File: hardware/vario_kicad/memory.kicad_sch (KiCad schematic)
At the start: 10 parts, among them U3 W25Q128JVS

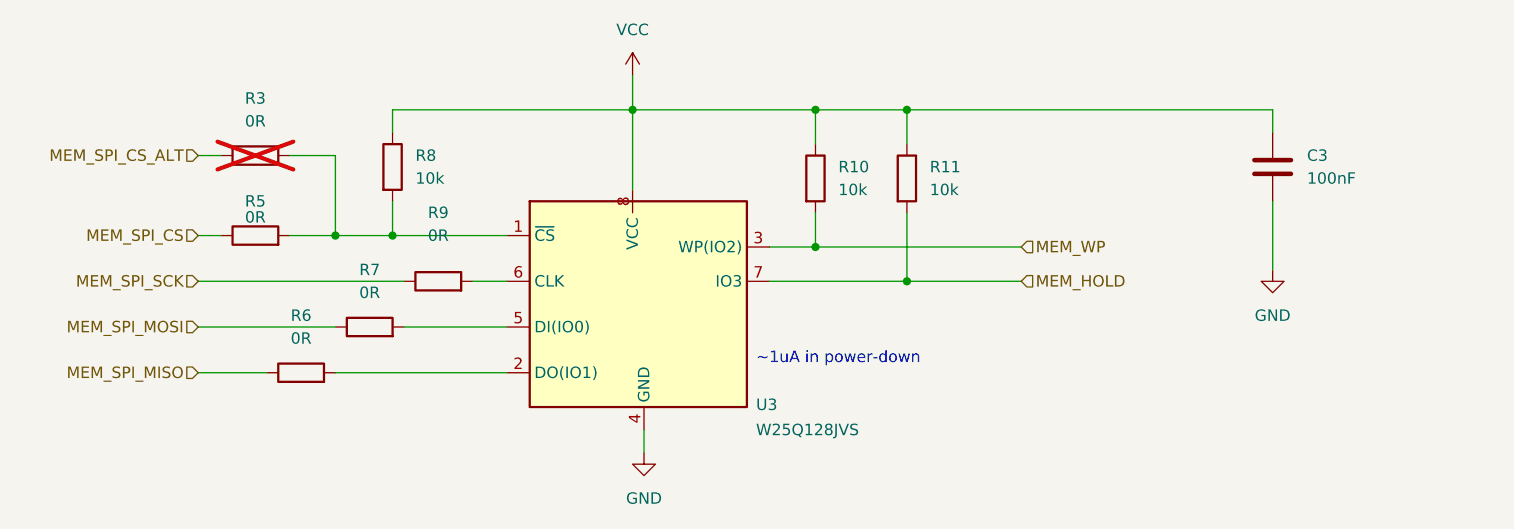
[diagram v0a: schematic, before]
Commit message: update footprints, add LSE oscillator
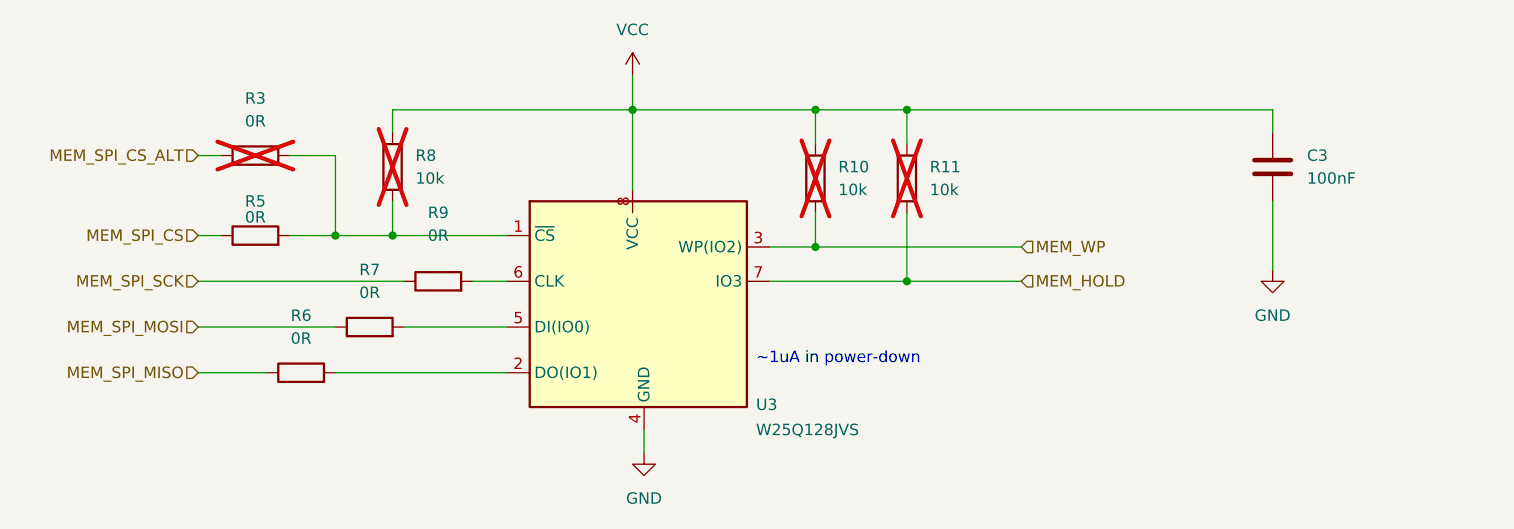
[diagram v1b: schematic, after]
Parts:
- R10, R11, R8: footprint (none) -> Resistor_SMD:R_0402_1005Metric; now not fitted
- R3, R5, R6, R7, R9: footprint (none) -> Resistor_SMD:R_0402_1005Metric
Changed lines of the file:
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@@
 			)
 		)
-		(property "Footprint" ""
+		(property "Footprint" "Resistor_SMD:R_0402_1005Metric"
 			(at 99.06 88.138 90)
 			(effects
@@
 		(in_bom yes)
 		(on_board yes)
-		(dnp no)
+		(dnp yes)
 		(fields_autoplaced yes)
 		(property "Reference" "R10"
@@
 			)
 		)
-		(property "Footprint" ""
+		(property "Footprint" "Resistor_SMD:R_0402_1005Metric"
 			(at 159.512 88.9 90)
 			(effects
@@
 		(in_bom yes)
 		(on_board yes)
-		(dnp no)
+		(dnp yes)
 		(fields_autoplaced yes)
 		(property "Reference" "R8"
@@
 			)
 		)
-		(property "Footprint" ""
+		(property "Footprint" "Resistor_SMD:R_0402_1005Metric"
 			(at 112.522 87.63 90)
 			(effects
@@
 			)
 		)
-		(property "Footprint" ""
+		(property "Footprint" "Resistor_SMD:R_0402_1005Metric"
 			(at 119.38 102.108 90)
 			(effects
@@
 			)
 		)
-		(property "Footprint" ""
+		(property "Footprint" "Resistor_SMD:R_0402_1005Metric"
 			(at 99.06 97.028 90)
 			(effects
@@
 		(in_bom yes)
 		(on_board yes)
-		(dnp no)
+		(dnp yes)
 		(fields_autoplaced yes)
 		(property "Reference" "R11"
@@
 			)
 		)
-		(property "Footprint" ""
+		(property "Footprint" "Resistor_SMD:R_0402_1005Metric"
 			(at 169.672 88.9 90)
 			(effects
@@
 			)
 		)
-		(property "Footprint" ""
+		(property "Footprint" "Resistor_SMD:R_0402_1005Metric"
 			(at 104.14 112.268 90)
 			(effects
@@
 			)
 		)
-		(property "Footprint" ""
+		(property "Footprint" "Resistor_SMD:R_0402_1005Metric"
 			(at 111.76 107.188 90)
 			(effects

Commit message: minor update to memory, untested
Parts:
- R8: now fitted
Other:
- moved on the sheet: U3
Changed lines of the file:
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@@
+	(wire
+		(pts
+			(xy 140.97 81.28) (xy 140.97 88.9)
+		)
+		(stroke
+			(width 0)
+			(type default)
+		)
+	)
 	(wire
 		(pts
@@
 		(pts
 			(xy 140.97 81.28) (xy 161.29 81.28)
-		)
-		(stroke
-			(width 0)
-			(type default)
-		)
-	)
-	(wire
-		(pts
-			(xy 140.97 81.28) (xy 140.97 90.17)
 		)
 		(stroke
@@
 		(in_bom yes)
 		(on_board yes)
-		(dnp yes)
+		(dnp no)
 		(fields_autoplaced yes)
 		(property "Reference" "R8"
@@
 			)
 		)
-		(property "Datasheet" "https://www.winbond.com/resource-files/w25q128jv_dtr%20revc%2003272018%20plus.pdf"
+		(property "Datasheet" "https://www.lcsc.com/product-detail/NOR-FLASH_Winbond-Elec-W25Q128JVSIQ_C113767.html"
 			(at 137.16 77.47 0)
 			(effects
@@
 			)
 		)
-		(property "Description" "128Mb Serial Flash Memory, Standard/Dual/Quad SPI, SOIC-8"
+		(property "Description" ""
 			(at 137.16 74.93 0)
 			(effects

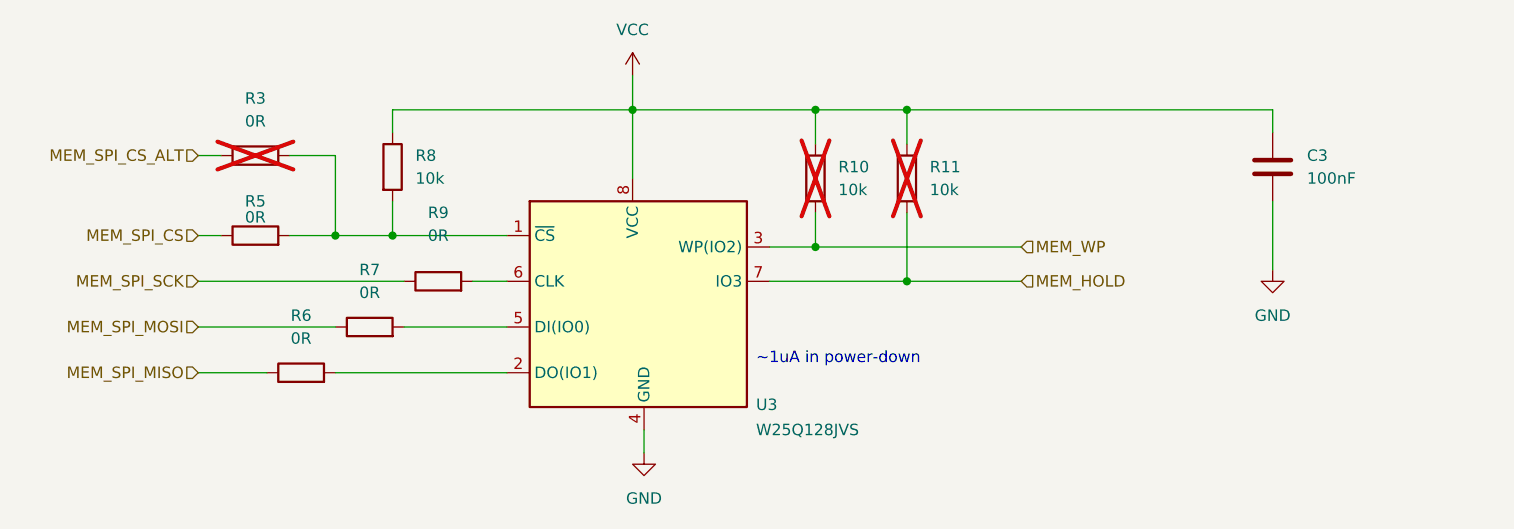
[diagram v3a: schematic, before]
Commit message: fix memory schematic, update button switches
- fix miso/mosi mistake: miso->miso, mosi->mosi
- WKUP1 needs a rising edge to wake up the MCU, so all switch logic was
  reversed
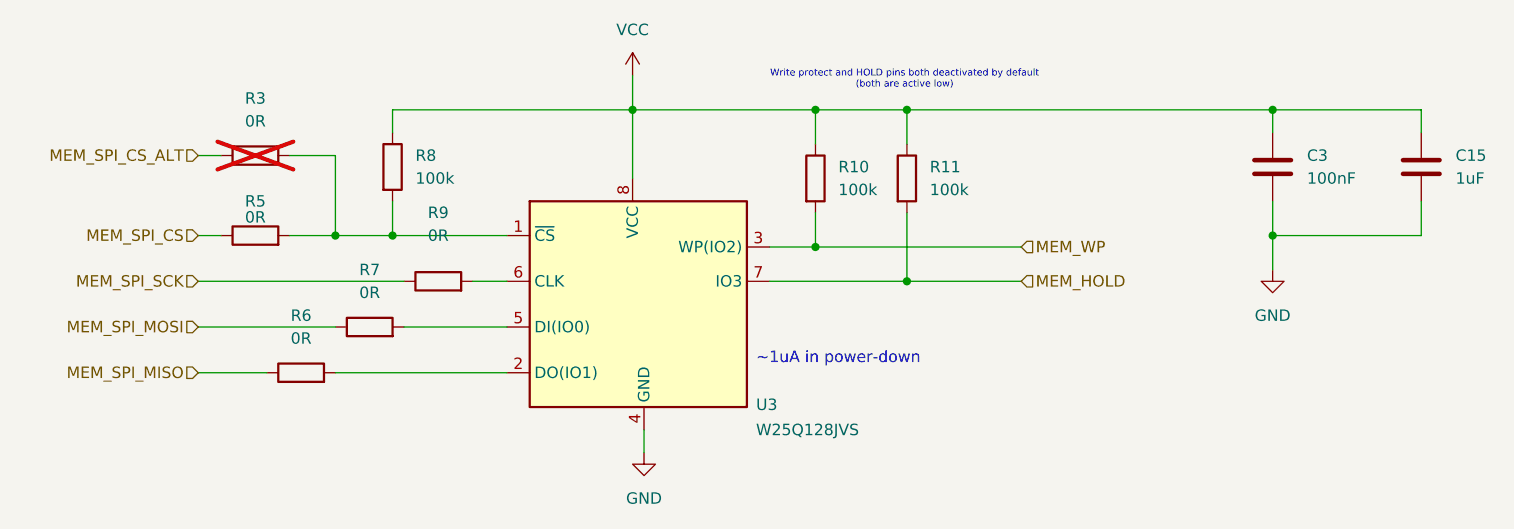
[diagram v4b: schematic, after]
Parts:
- added C15: 1uF, Capacitor_SMD:C_0603_1608Metric, symbol Device:C
- R10, R11: value 10k -> 100k; now fitted
- R8: value 10k -> 100k
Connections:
- net GND: now also C15.2
- net VCC: now also C15.1
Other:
- note added: "Write protect and HOLD pins both deactivated by default (both are active low)"
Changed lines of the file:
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@@
 	(paper "A4")
+	(junction
+		(at 212.09 95.25)
+		(diameter 0)
+		(color 0 0 0 0)
+	)
 	(junction
 		(at 161.29 96.52)
@@
 	)
 	(junction
+		(at 212.09 81.28)
+		(diameter 0)
+		(color 0 0 0 0)
+	)
+	(junction
 		(at 171.45 81.28)
 		(diameter 0)
@@
 	(wire
 		(pts
+			(xy 228.6 95.25) (xy 228.6 91.44)
+		)
+		(stroke
+			(width 0)
+			(type default)
+		)
+	)
+	(wire
+		(pts
 			(xy 114.3 81.28) (xy 114.3 83.82)
 		)
@@
 	(wire
 		(pts
+			(xy 212.09 95.25) (xy 228.6 95.25)
+		)
+		(stroke
+			(width 0)
+			(type default)
+		)
+	)
+	(wire
+		(pts
 			(xy 212.09 81.28) (xy 212.09 83.82)
 		)
@@
 	(wire
 		(pts
+			(xy 212.09 95.25) (xy 212.09 99.06)
+		)
+		(stroke
+			(width 0)
+			(type default)
+		)
+	)
+	(wire
+		(pts
 			(xy 114.3 81.28) (xy 140.97 81.28)
 		)
@@
 	(wire
 		(pts
+			(xy 212.09 81.28) (xy 228.6 81.28)
+		)
+		(stroke
+			(width 0)
+			(type default)
+		)
+	)
+	(wire
+		(pts
 			(xy 171.45 81.28) (xy 171.45 85.09)
 		)
@@
 	(wire
 		(pts
+			(xy 228.6 81.28) (xy 228.6 83.82)
+		)
+		(stroke
+			(width 0)
+			(type default)
+		)
+	)
+	(wire
+		(pts
 			(xy 140.97 77.47) (xy 140.97 81.28)
 		)
@@
 	(wire
 		(pts
-			(xy 212.09 91.44) (xy 212.09 99.06)
+			(xy 212.09 91.44) (xy 212.09 95.25)
 		)
 		(stroke
@@
 			(width 0)
 			(type default)
+		)
+	)
+	(text "Write protect and HOLD pins both deactivated by default \n(both are active low)"
+		(exclude_from_sim no)
+		(at 171.196 77.978 0)
+		(effects
+			(font
+				(size 0.762 0.762)
+			)
 		)
 	)
@@
 		(in_bom yes)
 		(on_board yes)
-		(dnp yes)
+		(dnp no)
 		(fields_autoplaced yes)
 		(property "Reference" "R10"
@@
 			)
 		)
-		(property "Value" "10k"
+		(property "Value" "100k"
 			(at 163.83 90.1699 0)
 			(effects
@@
 			)
 		)
-		(property "Value" "10k"
+		(property "Value" "100k"
 			(at 116.84 88.8999 0)
 			(effects
@@
 				(path "/50389aff-b244-451e-8e3a-c5addd2215e1/46f26a35-4266-4bb4-816f-d8c91119a86f"
 					(reference "R8")
+					(unit 1)
+				)
+			)
+		)
+	)
+	(symbol
+		(lib_id "Device:C")
+		(at 228.6 87.63 0)
+		(unit 1)
+		(exclude_from_sim no)
+		(in_bom yes)
+		(on_board yes)
+		(dnp no)
+		(fields_autoplaced yes)
+		(property "Reference" "C15"
+			(at 232.41 86.3599 0)
+			(effects
+				(font
+					(size 1.27 1.27)
+				)
+				(justify left)
+			)
+		)
+		(property "Value" "1uF"
+			(at 232.41 88.8999 0)
+			(effects
+				(font
+					(size 1.27 1.27)
+				)
+				(justify left)
+			)
+		)
+		(property "Footprint" "Capacitor_SMD:C_0603_1608Metric"
+			(at 229.5652 91.44 0)
+			(effects
+				(font
+					(size 1.27 1.27)
+				)
+				(hide yes)
+			)
+		)
+		(property "Datasheet" "~"
+			(at 228.6 87.63 0)
+			(effects
+				(font
+					(size 1.27 1.27)
+				)
+				(hide yes)
+			)
+		)
+		(property "Description" "Unpolarized capacitor"
+			(at 228.6 87.63 0)
+			(effects
+				(font
+					(size 1.27 1.27)
+				)
+				(hide yes)
+			)
+		)
+		(pin "1"
+		)
+		(pin "2"
+		)
+		(instances
+			(project ""
+				(path "/50389aff-b244-451e-8e3a-c5addd2215e1/46f26a35-4266-4bb4-816f-d8c91119a86f"
+					(reference "C15")
 					(unit 1)
 				)
@@
 		(in_bom yes)
 		(on_board yes)
-		(dnp yes)
+		(dnp no)
 		(fields_autoplaced yes)
 		(property "Reference" "R11"
@@
 			)
 		)
-		(property "Value" "10k"
+		(property "Value" "100k"
 			(at 173.99 90.1699 0)
 			(effects

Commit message: use 0402 instead of 0603 for almost all caps
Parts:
- C15, C3: footprint Capacitor_SMD:C_0603_1608Metric -> Capacitor_SMD:C_0402_1005Metric
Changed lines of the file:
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@@
 			)
 		)
-		(property "Footprint" "Capacitor_SMD:C_0603_1608Metric"
+		(property "Footprint" "Capacitor_SMD:C_0402_1005Metric"
 			(at 213.0552 91.44 0)
 			(effects
@@
 			)
 		)
-		(property "Footprint" "Capacitor_SMD:C_0603_1608Metric"
+		(property "Footprint" "Capacitor_SMD:C_0402_1005Metric"
 			(at 229.5652 91.44 0)
 			(effects
